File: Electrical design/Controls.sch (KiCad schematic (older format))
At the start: 11 parts

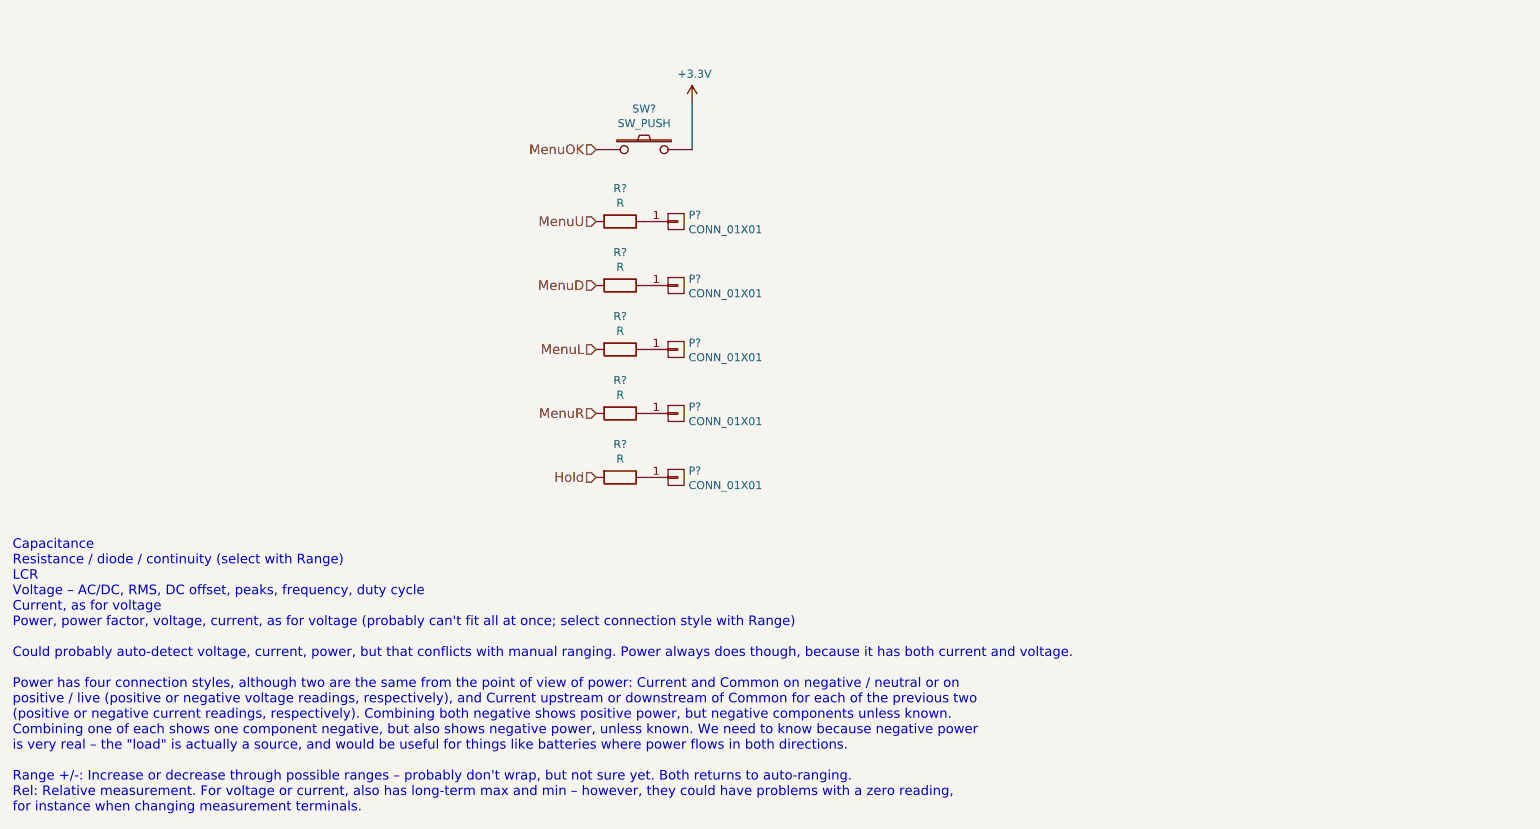
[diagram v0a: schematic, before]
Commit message: Updated schematics.
Added speaker / buzzer, reset circuit (battery under-voltage lockout), changed battery charger IC.
Altered Vout circuit.
Added most resistor / capacitor values (those missing are either dependent on battery thermistor or ADC).
Updated to show "correct" op-amps.
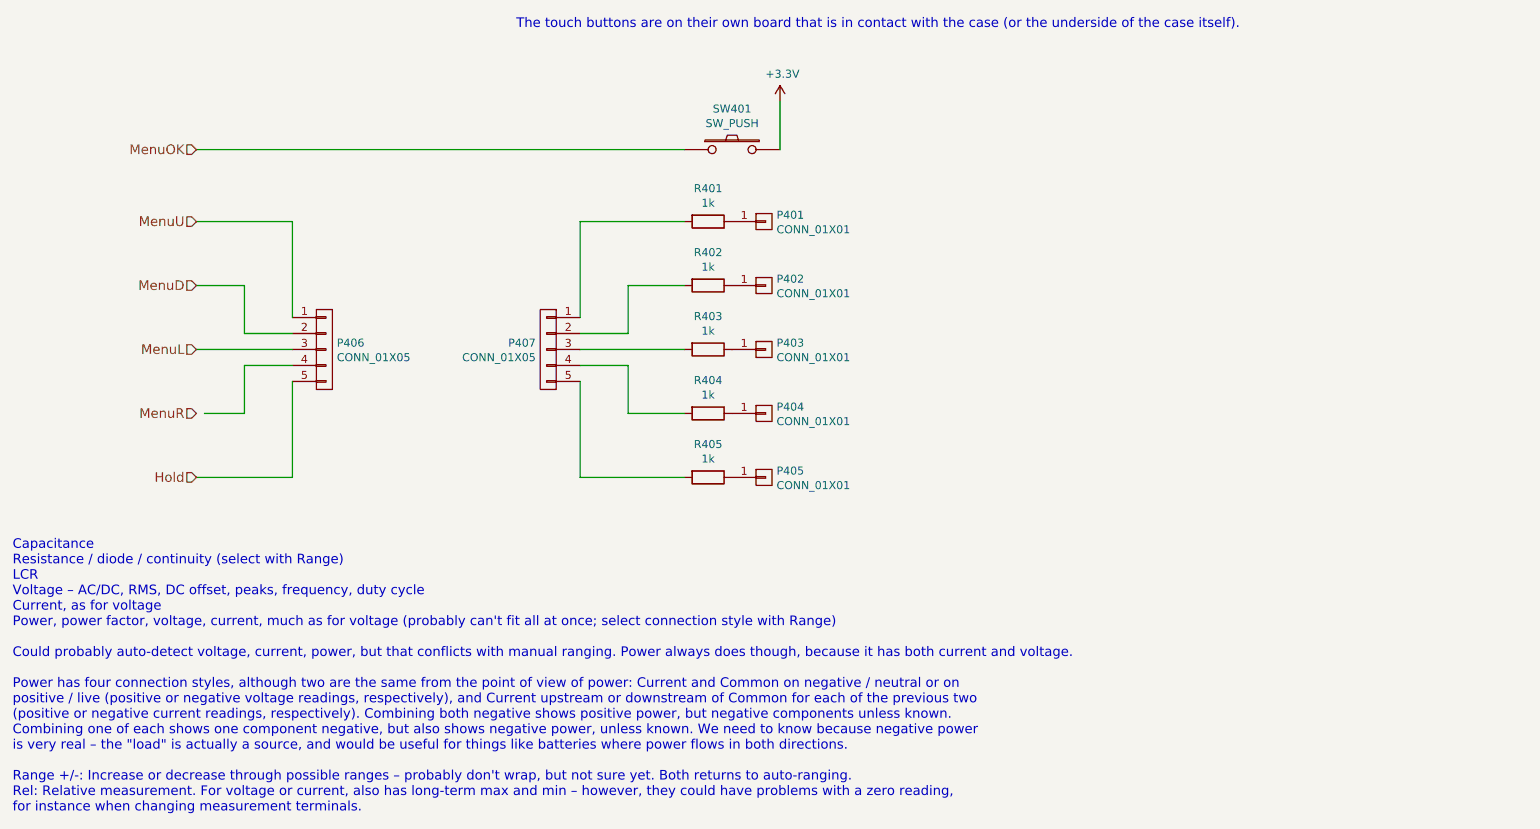
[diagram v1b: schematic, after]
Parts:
- added P406, P407: CONN_01X05, Pin_Headers:Pin_Header_Straight_1x05, symbol CONN_01X05
- P401, P402, P403, P404, P405: renamed from P?; footprint (none) -> Wire_Pads:SolderWirePad_single_SMD_5x10mm
- R401, R402, R403, R404, R405: renamed from R?; value R -> 1k; footprint (none) -> my footprints:SMDuniversal_0603to1210_HandSoldering
- SW401: renamed from SW?; footprint (none) -> Buttons_Switches_ThroughHole:SW_PUSH_SMALL
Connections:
- wire segments 1 -> 24
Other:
- note added: "Capacitance\nResistance / diode / continuity (select with Range)\nLCR\nVoltage – AC/DC, RMS, DC offset, peaks, frequency, duty cycle\nCurrent, as for voltage\nPower, power factor, voltage, current, much as for voltage (probably can't fit all at once; select connection style with Range)\n\nCould probably auto-detect voltage, current, power, but that conflicts with manual ranging. Power always does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"
- note added: "The touch buttons are on their own board that is in contact with the case (or the underside of the case itself)."
- note removed: "Capacitance\nResistance / diode / continuity (select with Range)\nLCR\nVoltage – AC/DC, RMS, DC offset, peaks, frequency, duty cycle\nCurrent, as for voltage\nPower, power factor, voltage, current, as for voltage (probably can't fit all at once; select connection style with Range)\n\nCould probably auto-detect voltage, current, power, but that conflicts with manual ranging. Power always does thou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"
- moved on the sheet: P401, P402, P403, P404, P405, R401, R402, R403, R404, R405, SW401

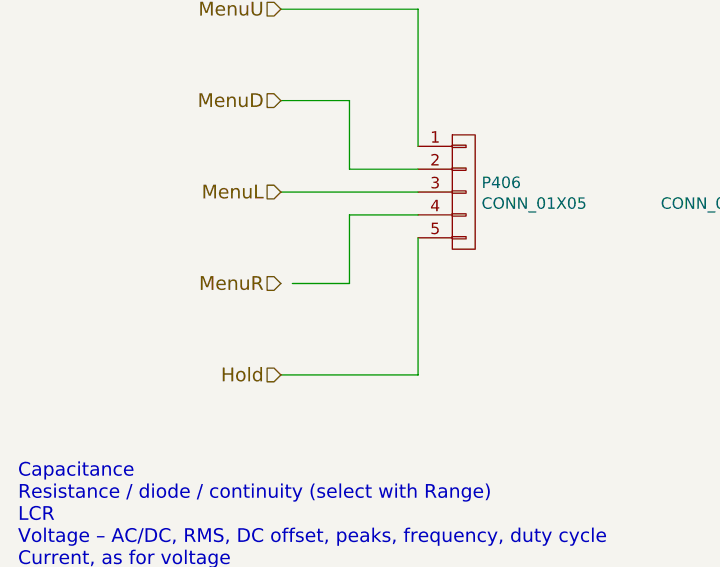
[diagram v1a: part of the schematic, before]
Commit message: Add battery voltage monitoring.
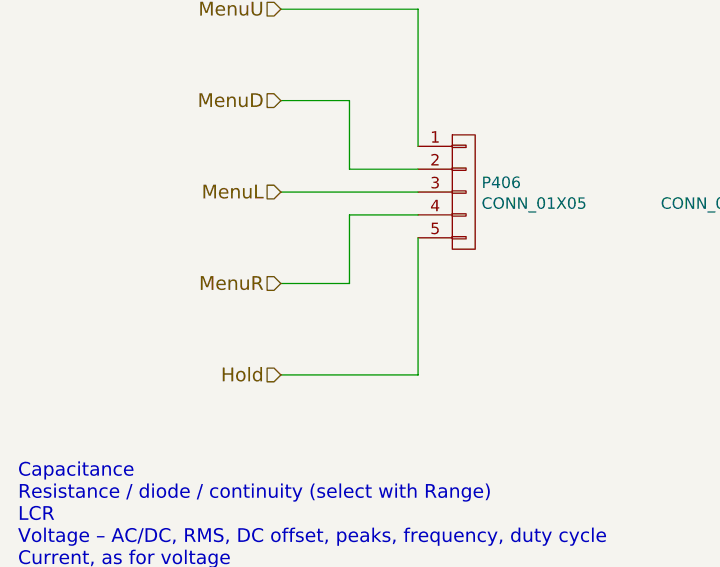
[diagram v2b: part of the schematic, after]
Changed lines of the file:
@@
 Capacitance\nResistance / diode / continuity (select with Range)\nLCR\nVoltage – AC/DC, RMS, DC offset, peaks, frequency, duty cycle\nCurrent, as for voltage\nPower, power factor, voltage, current, much as for voltage (probably can't fit all at once; select connection style with Range)\n\nCould probably auto-detect voltage, current, power, but that conflicts with manual ranging. Power always does though, because it has both current and voltage.\n\nPower has four connection styles, although two are the same from the point of view of power: Current and Common on negative / neutral or on\npositive / live (positive or negative voltage readings, respectively), and Current upstream or downstream of Common for each of the previous two\n(positive or negative current readings, respectively). Combining both negative shows positive power, but negative components unless known.\nCombining one of each shows one component negative, but also shows negative power, unless known. We need to know because negative power\nis very real – the "load" is actually a source, and would be useful for things like batteries where power flows in both directions.\n\nRange +/-: Increase or decrease through possible ranges – probably don't wrap, but not sure yet. Both returns to auto-ranging.\nRel: Relative measurement. For voltage or current, also has long-term max and min – however, they could have problems with a zero reading,\nfor instance when changing measurement terminals.
 $Comp
-L +3.3V #PWR401
+L +3.3V #PWR065
 U 1 1 5747A41F
 P 6350 1700
-F 0 "#PWR401" H 6350 1550 50  0001 C CNN
+F 0 "#PWR065" H 6350 1550 50  0001 C CNN
 F 1 "+3.3V" H 6365 1873 50  0000 C CNN
 F 2 "" H 6350 1700 50  0000 C CNN
@@
 	3300 4050 2700 4050
 Wire Wire Line
-	2750 3650 3000 3650
+	2700 3650 3000 3650
 Wire Wire Line
 	3000 3650 3000 3350
